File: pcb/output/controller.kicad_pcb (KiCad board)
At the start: 2 copper layers, 100 x 80 mm, 54 parts, among them J1 DC_BARREL_2.1x5.5mm, J10 USB-C_Receptacle, J11 TMC2209_Header, J12 SWD_Header, J2 KSD9700_100C_NC, J3 ScrewTerm_SSR_Ctrl, J4 ScrewTerm_Fan, J5 ScrewTerm_Solenoid, J6 JST_SHT40, J7 JST_MHZ19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

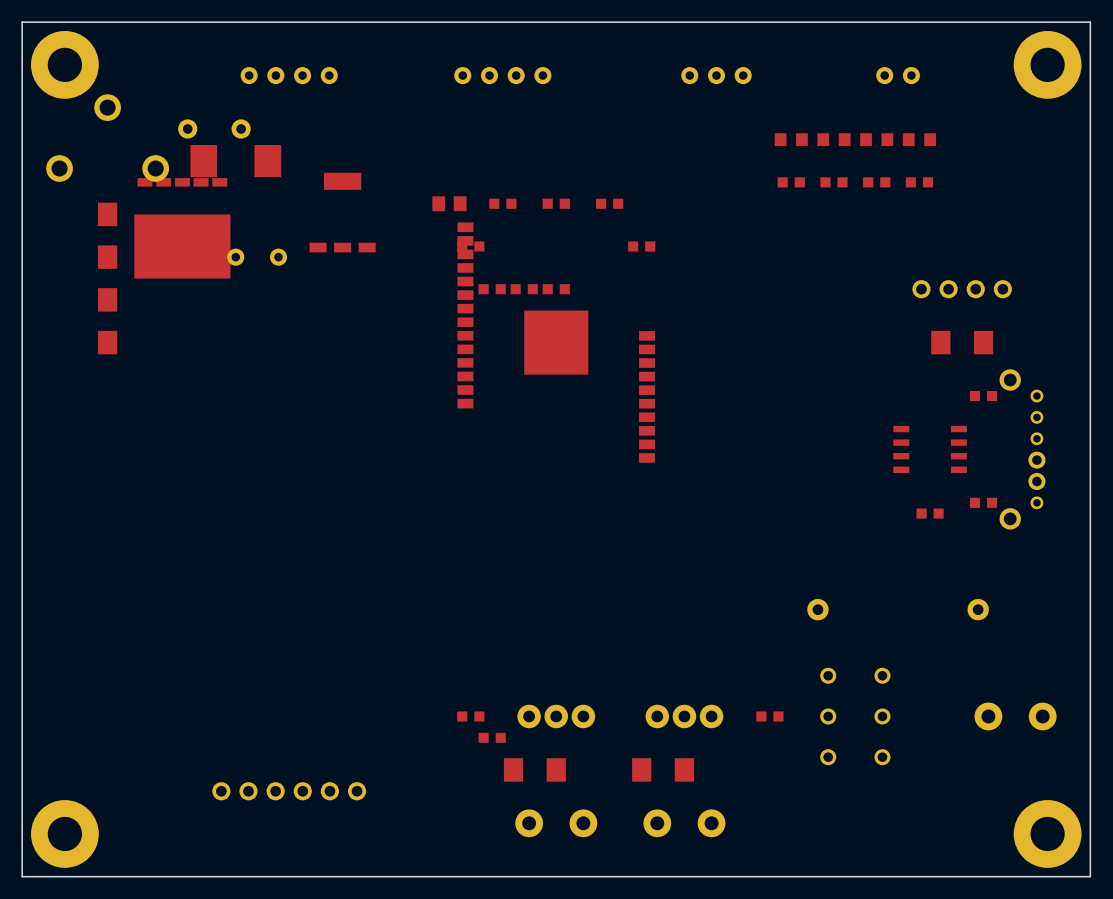
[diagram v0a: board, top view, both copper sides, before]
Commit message: fix(controller-pcb): v2 — placement corrected, re-exported DSN, Freerouting converged, DRC clean
Fixed 4 component placement bugs that caused v1 DRC failures:
- R1, R2 (10K pull-ups): (42/58, 21) -> (42/58, 43), clears U1 ESP32-S3 pad row
- J1 (barrel jack): (8, 8) -> (10, 5), clears U2 LM2596 pad row by 3.15mm
- L1 (33uH inductor): (20, 13) -> (27, 11), clears U2 pad row and C1 pad 2
- C2 (220uF output cap): (22, 22) -> (25, 28), clears U2 TAB by 2.7mm in x
- C1 (220uF input cap): (18, 10) -> (36, 10), clears J1 pad 3 after J1 move

Added GND copper-pour zones on F.Cu and B.Cu to the KiCad PCB writer so
DRC can see GND plane connectivity (previously only in DSN, not kicad_pcb).
connect_pads yes / min_thickness 0.15 avoids starved-thermal errors on
TAB pads (U1 center paddle, U2 TO-263 tab, J10 USB-C shield).

Freerouting 2.1.0 headless NPE was caused by the 4 placement overlaps —
once fixed, routing converged in <30s:
  - 194 traces, 40 vias, 0 unconnected, 0 clearance violations
  - SES round-tripped via --from-ses --validate
  - Final DRC: 0 errors, 1 unconnected (F.Cu GND zone split into 2
    islands by routed traces; B.Cu solid plane + vias provide full
    GND connectivity — non-critical).

Fab package controller_jlcpcb_v2.zip (103 KB) ready for JLCPCB upload.
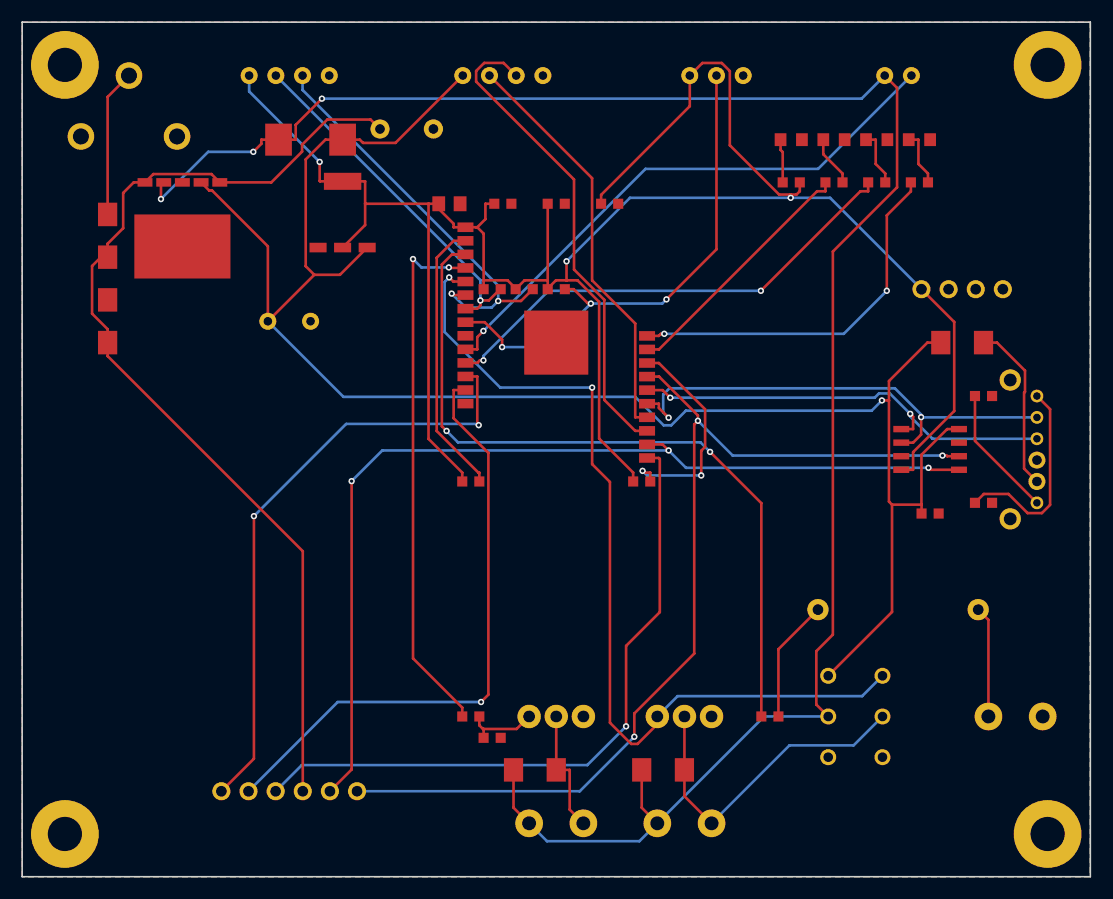
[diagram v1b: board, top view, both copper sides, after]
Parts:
- moved R1 22.0 mm to (42.0, 43.0)
- moved R2 22.0 mm to (58.0, 43.0)
- moved C1 18.0 mm to (36.0, 10.0)
- moved L1 7.28 mm to (27.0, 11.0)
- moved C2 6.71 mm to (25.0, 28.0)
- moved J1 3.61 mm to (10.0, 5.00)
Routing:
- net +3V3: track 0.00 -> 210.1 mm, vias 0 -> 3
- net +12V: track 0.00 -> 184.1 mm, vias 0 -> 3
- net +5V: track 0.00 -> 169.7 mm, vias 0 -> 1
- net +24V_SW: track 0.00 -> 94.3 mm
- net TMC_UART_RX: track 0.00 -> 92.7 mm, vias 0 -> 3
- net TMC_UART_TX: track 0.00 -> 90.9 mm, vias 0 -> 3
- net CO2_SOL_PWM: track 0.00 -> 84.4 mm, vias 0 -> 2
- net HEATER_SSR_MCU: track 0.00 -> 70.6 mm, vias 0 -> 2
- net EN_N: track 0.00 -> 62.9 mm, vias 0 -> 1
- net STEP: track 0.00 -> 57.4 mm, vias 0 -> 2
- net DIR: track 0.00 -> 57.2 mm, vias 0 -> 1
- net WINDOW_HEATER: track 0.00 -> 53.0 mm, vias 0 -> 1
- net FAN_PWM: track 0.00 -> 50.0 mm, vias 0 -> 2
- net DS18B20_DATA: track 0.00 -> 47.9 mm, vias 0 -> 3
- net MHZ19_RX: track 0.00 -> 45.5 mm
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- added copper zone on B.Cu, net GND
- added copper zone on F.Cu, net GND
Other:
- net class Default removed
